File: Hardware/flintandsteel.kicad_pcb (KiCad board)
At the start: 4 copper layers, 44 x 58 mm, 117 parts, among them J1 RBUS, J2 USB_C_Receptacle_USB2.0, J3 Conn_01x02_Male, J4 Conn_01x02_Male, J5 Conn_01x02_Male, J6 Conn_01x02_Male, Q1 BUK9M11-40EX, Q2 BUK9M11-40EX, Q3 BUK9M11-40EX, Q4 BUK9M11-40EX, U1 ESP32-S3, U2 SN65HVD230, U3 LM66200DRLR, U4 MAX77827AEFD+T, U5 SC4215, U6 LTV-247, U7 INA219AxDCN, Y1 R940000171

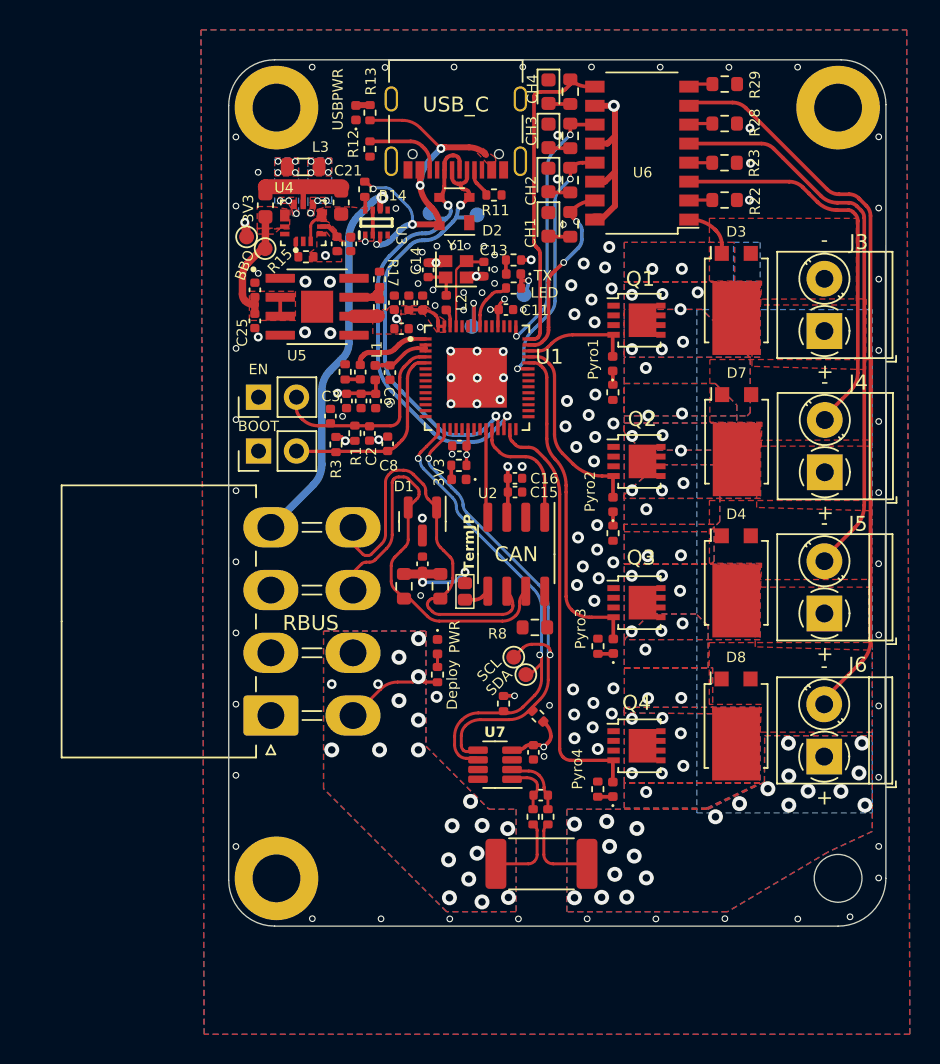
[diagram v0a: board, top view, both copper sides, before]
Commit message: added high side switch
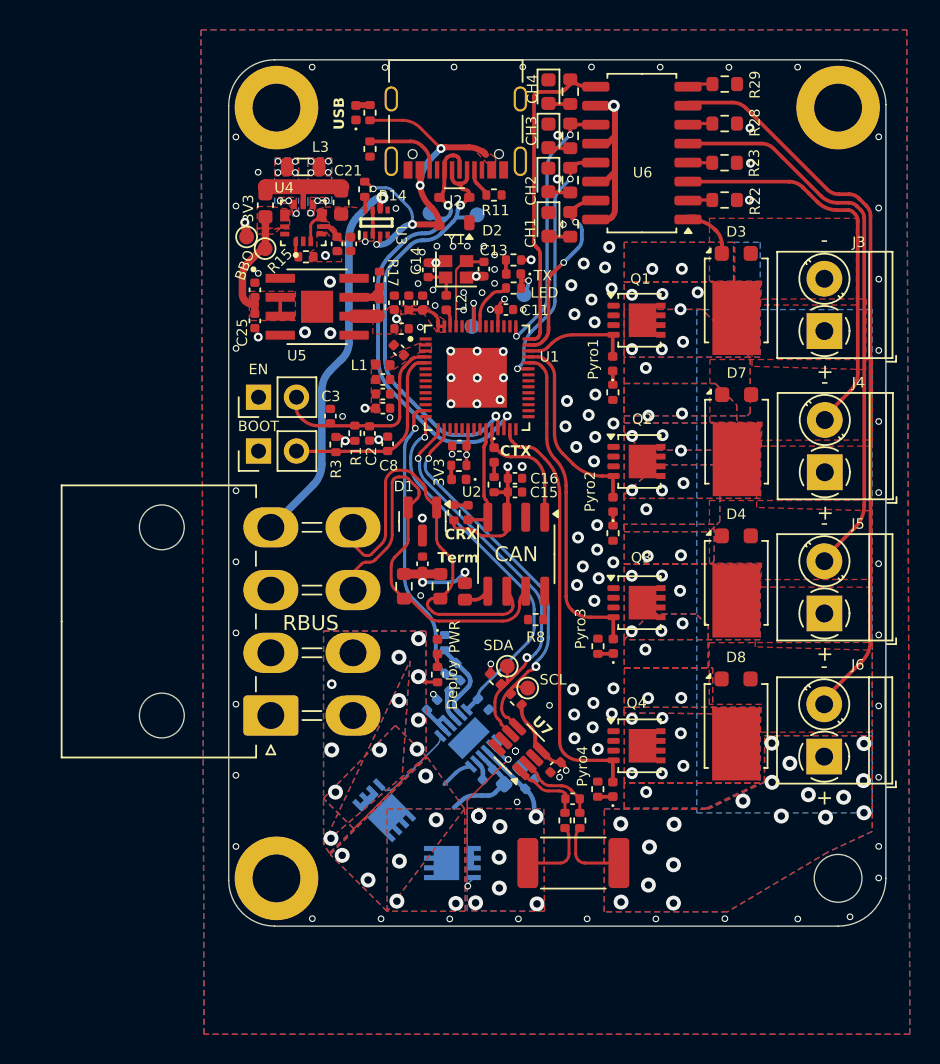
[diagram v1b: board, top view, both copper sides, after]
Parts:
- added C28: 0.1uF, Capacitor_SMD:C_0603_1608Metric, B.Cu at (125.0, 114.9)
- added C29: 0.1uF, Capacitor_SMD:C_0402_1005Metric, B.Cu at (119.6, 110.2)
- added C30: 0.1uF, Capacitor_SMD:C_0402_1005Metric, B.Cu at (126.2, 115.5)
- added CANRXLED1: ORANGE_LED, LED_SMD:LED_0402_1005Metric, F.Cu at (122.0, 97.3)
- added CANTXLED1: GREEN_LED, LED_SMD:LED_0402_1005Metric, F.Cu at (123.8, 93.5)
- added Q5: BSZ025N04LS, iclr:BSZ025N04LS, B.Cu at (116.4, 117.2)
- added Q6: BSZ025N04LS, iclr:BSZ025N04LS, B.Cu at (121.0, 120.8)
- added R30: 1k, Resistor_SMD:R_0402_1005Metric, F.Cu at (121.1, 97.3)
- added R37: R_Small, Resistor_SMD:R_0402_1005Metric, B.Cu at (121.1, 108.9)
- added R38: R_Small, Resistor_SMD:R_0402_1005Metric, B.Cu at (120.9, 107.7)
- added R39: R_Small, Resistor_SMD:R_0402_1005Metric, B.Cu at (120.5, 106.0)
- added R7: 1k, Resistor_SMD:R_0402_1005Metric, F.Cu at (123.8, 95.4)
- added U8: LM74810, iclr:SON50P300X300X80-13N-D, B.Cu at (122.1, 112.4)
- C12: value DNP -> 1uF; moved to B.Cu
- J2: footprint Connector_USB:USB_C_Receptacle_Palconn_UTC16-G -> iclr:USB_C_Receptacle_Palconn_UTC16-G
- R5: value DNP -> 10k; moved to B.Cu
- R8: footprint Resistor_SMD:R_0603_1608Metric -> Resistor_SMD:R_0402_1005Metric
- USBLED1: footprint Diode_SMD:D_0402_1005Metric -> LED_SMD:LED_0402_1005Metric
- Y1: footprint Crystal:Crystal_SMD_2016-4Pin_2.0x1.6mm -> iclr:Crystal_SMD_2016-4Pin_2.0x1.6mm
- moved C12 28.3 mm to (123.4, 114.9), turned to -135 degrees
- moved R5 24.1 mm to (123.0, 110.1), turned to -45 degrees
- moved C1 2.48 mm to (116.3, 90.3), turned to 0 degrees
- moved TP3 2.27 mm to (126.0, 109.1)
- moved C19 2.15 mm to (129.0, 116.5)
- moved R34 2.15 mm to (128.5, 117.9)
- moved R35 2.15 mm to (129.5, 117.9)
- moved R33 2.14 mm to (129.1, 120.8)
- moved U7 1.93 mm to (125.5, 113.1), turned to 135 degrees
- moved R32 1.83 mm to (125.2, 109.8)
- moved C18 1.79 mm to (127.9, 114.4), turned to -135 degrees
- moved R31 1.75 mm to (123.9, 108.4), turned to -45 degrees
- moved C6 1.61 mm to (117.4, 86.4), turned to 135 degrees
- moved C4 1.53 mm to (116.3, 89.4), turned to 0 degrees
- moved C5 1.52 mm to (116.3, 88.4), turned to 0 degrees
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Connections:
- net Net-(U7-IN+) renamed /SHNT_IN+
- net Net-(U7-IN-) renamed /SHNT_IN-
- C12 pad 1: Net-(C12-Pad1) -> /High side master switch/C
- C12 pad 2: Net-(U1-LNA_IN/RF) -> /High side master switch/CAP
- R33 pad 1: /DeployV -> /DeployV_Post_Diode
- R34 pad 1: /DeployV -> /DeployV_Post_Diode
- R5 pad 1: GND -> /HSIDE_EN
- R5 pad 2: Net-(C12-Pad1) -> GND
- U1 pad 1: Net-(U1-LNA_IN/RF) -> unconnected-(U1-LNA_IN/RF-Pad1)
- U1 pad 13: unconnected-(U1-GPIO8/ADC1_CH7-Pad13) -> /BUS_VMON
- U1 pad 14: unconnected-(U1-GPIO9/ADC1_CH8-Pad14) -> /HSIDE_EN
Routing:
- net /HSIDE_EN: track 0.00 -> 25.1 mm, vias 0 -> 1
- net /BUS_VMON: track 0.00 -> 20.4 mm, vias 0 -> 1
- net /High side master switch/HGate: track 0.00 -> 11.8 mm, vias 0 -> 2
- net /DeployV_Post_Diode: track 0.00 -> 11.0 mm, vias 0 -> 8
- net /High side master switch/C: track 0.00 -> 9.11 mm, vias 0 -> 7
- net /SCL: track 34.2 -> 26.4 mm
- net /DeployV: track 12.0 -> 5.45 mm, vias 20 -> 11
- net /High side master switch/DGate: track 0.00 -> 5.91 mm
- net Net-(U8-OV): track 0.00 -> 5.45 mm
- net +3V3: track 37.9 -> 43.1 mm
- net Net-(U1-LNA_IN/RF): track 5.21 -> 0.00 mm
- net /SDA: track 32.5 -> 27.5 mm
- net Net-(C6-Pad1): track 4.66 -> 0.00 mm
- net Net-(U8-SW): track 0.00 -> 2.22 mm
- net /CAN_RX: track 5.77 -> 7.39 mm
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- added copper zone on B.Cu, net /DeployV_Post_Diode
- added copper zone on F.Cu, net /DeployV_Post_Diode
- added copper zone on B.Cu, net /High side master switch/C
- added copper zone on F.Cu, net /High side master switch/C
- added copper zone on F.Cu, net Net-(C6-Pad1)
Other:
- board text added: "CRX"
- board text added: "CTX"
- board text added: "Designed By Andrei Paduraru Electronics 2024"
- board text added: "FLINT & STEEL v3.0"
- board text added: "USB"
- board text removed: "Designed By Andrei Paduraru Electronics and Payload 2023"
- board text removed: "locked"

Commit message: v3 hardware I guess
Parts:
- added 16VLED2: ORANGE_LED, LED_SMD:LED_0402_1005Metric, F.Cu at (143.0, 123.5)
- added D11: S-102T, iclr:SODFL3516X70N, F.Cu at (140.1, 68.8)
- added D12: S-102T, iclr:SODFL3516X70N, F.Cu at (140.1, 73.8)
- added D13: S-102T, iclr:SODFL3516X70N, F.Cu at (140.1, 76.5)
- added D14: S-102T, iclr:SODFL3516X70N, F.Cu at (140.1, 71.3)
- added D15: V8PAM10S-M3/I, iclr:V8PAM10SM3I, B.Cu at (143.0, 93.3)
- added D16: V8PAM10S-M3/I, iclr:V8PAM10SM3I, B.Cu at (143.0, 83.7)
- added D17: V8PAM10S-M3/I, iclr:V8PAM10SM3I, B.Cu at (142.9, 102.6)
- added D18: V8PAM10S-M3/I, iclr:V8PAM10SM3I, B.Cu at (142.9, 112.2)
- added G***: LOGO, iclr:rae_logo_4mm, F.Cu at (109.2, 116.3)
- added G***: LOGO, iclr:rae_logo_8mm, B.Cu at (135.9, 110.3)
- added R40: 3k, Resistor_SMD:R_0402_1005Metric, F.Cu at (141.0, 123.1)
- Q1, Q2, Q3, Q4: value BUK9M11-40EX -> BSZ025N04LS; footprint Package_TO_SOT_SMD:LFPAK33 -> iclr:BSZ025N04LS
- R22, R23, R28, R29: value 10k -> 10K; footprint Resistor_SMD:R_0603_1608Metric -> Resistor_SMD:R_0402_1005Metric
- moved R28 44.1 mm to (129.8, 114.4), turned to -90 degrees
- moved R29 37.4 mm to (129.9, 104.8), turned to -90 degrees
- moved G*** 34.3 mm to (112.6, 83.1)
- moved R23 24.4 mm to (130.7, 96.8), turned to -90 degrees
- moved R22 12.9 mm to (130.5, 85.9), turned to -90 degrees
- moved G*** 0.30 mm to (130.5, 90.7)
- turned Q1 to -90 degrees
- turned Q2 to -90 degrees
- turned Q3 to -90 degrees
- turned Q4 to -90 degrees
- renumbered D5 to D10, D10 to D5, D9 to D6, D6 to D9, R27 to R20, R26 to R21, R21 to R26, R20 to R27
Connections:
- net /Cont 4 renamed /Cont 0
- D3 pad 1: Net-(J3-Pin_2) -> Net-(D16-A)
- D3 pad 2: Net-(J3-Pin_2) -> Net-(D16-A)
- D4 pad 1: Net-(J5-Pin_2) -> Net-(D17-A)
- D4 pad 2: Net-(J5-Pin_2) -> Net-(D17-A)
- D7 pad 1: Net-(J4-Pin_2) -> Net-(D15-A)
- D7 pad 2: Net-(J4-Pin_2) -> Net-(D15-A)
- D8 pad 1: Net-(J6-Pin_2) -> Net-(D18-A)
- D8 pad 2: Net-(J6-Pin_2) -> Net-(D18-A)
- Firing1 pad 2: /Nuke 1 -> /Nuke 0
- Firing2 pad 2: /Nuke 2 -> /Nuke 1
- Firing3 pad 2: /Nuke 3 -> /Nuke 2
- Firing4 pad 2: /Nuke 4 -> /Nuke 3
- J3 pad 2: Net-(J3-Pin_2) -> Net-(D16-A)
- J4 pad 2: Net-(J4-Pin_2) -> Net-(D15-A)
- J5 pad 2: Net-(J5-Pin_2) -> Net-(D17-A)
- J6 pad 2: Net-(J6-Pin_2) -> Net-(D18-A)
- Q1 pad 4: /Nuke 1 -> /Nuke 0
- Q2 pad 4: /Nuke 2 -> /Nuke 1
- Q3 pad 4: /Nuke 3 -> /Nuke 2
- Q4 pad 4: /Nuke 4 -> /Nuke 3
- R21 pad 1: /Cont 3 -> /Cont 1
- R22 pad 1: Net-(R22-Pad1) -> /Nuke 0
- R23 pad 1: Net-(R23-Pad1) -> /Nuke 1
- R27 pad 1: /Cont 1 -> /Cont 3
- R28 pad 1: Net-(R28-Pad1) -> /Nuke 3
- R29 pad 1: Net-(R29-Pad1) -> /Nuke 2
- U1 pad 27: /Nuke 4 -> /Nuke 3
- U1 pad 38: /Nuke 3 -> /Nuke 2
- U1 pad 39: /Nuke 2 -> /Nuke 1
- U1 pad 40: /Nuke 1 -> /Nuke 0
- U1 pad 41: /Cont 1 -> /Cont 3
- U1 pad 43: /Cont 3 -> /Cont 1
- U6 pad 1: Net-(J3-Pin_2) -> Net-(D18-A)
- U6 pad 11: /Cont 3 -> /Cont 1
- U6 pad 15: /Cont 1 -> /Cont 3
- U6 pad 2: Net-(R22-Pad1) -> Net-(D13-A)
- U6 pad 3: Net-(J4-Pin_2) -> Net-(D17-A)
- U6 pad 4: Net-(R23-Pad1) -> Net-(D12-A)
- U6 pad 5: Net-(J5-Pin_2) -> Net-(D15-A)
- U6 pad 6: Net-(R28-Pad1) -> Net-(D14-A)
- U6 pad 7: Net-(J6-Pin_2) -> Net-(D16-A)
- U6 pad 8: Net-(R29-Pad1) -> Net-(D11-A)
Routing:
- net Net-(J6-Pin_2): track 49.2 -> 0.00 mm
- net Net-(D18-A): track 0.00 -> 48.5 mm, vias 0 -> 2
- net Net-(J5-Pin_2): track 37.5 -> 0.00 mm
- net Net-(D17-A): track 0.00 -> 37.1 mm, vias 0 -> 2
- net /Nuke 4: track 28.4 -> 0.00 mm
- net Net-(D15-A): track 0.00 -> 27.7 mm
- net Net-(J4-Pin_2): track 26.3 -> 0.00 mm
- net Net-(D16-A): track 0.00 -> 14.8 mm
- net /Nuke 2: track 13.1 -> 22.2 mm
- net /Nuke 0: track 0.00 -> 7.48 mm
- net /Nuke 1: track 7.48 -> 14.1 mm
- net /Nuke 3: track 22.2 -> 28.4 mm
- net /Cont 3: track 18.0 -> 12.8 mm
- net /Cont 1: track 12.8 -> 18.0 mm
- net Net-(J3-Pin_2): track 4.35 -> 0.00 mm
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- added copper zone on B.Cu, net Net-(D15-A)
- added copper zone on F.Cu, net Net-(D15-A)
- added copper zone on B.Cu, net Net-(D16-A)
- added copper zone on F.Cu, net Net-(D16-A)
- added copper zone on B.Cu, net Net-(D17-A)
- added copper zone on F.Cu, net Net-(D17-A)
- added copper zone on B.Cu, net Net-(D18-A)
- added copper zone on F.Cu, net Net-(D18-A)
- removed copper zone on F.Cu, net Net-(J3-Pin_2)
- removed copper zone on F.Cu, net Net-(J4-Pin_2)
- removed copper zone on F.Cu, net Net-(J5-Pin_2)
- removed copper zone on F.Cu, net Net-(J6-Pin_2)
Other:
- board text removed: "Batch Number - JLCJLCJLCJLC"

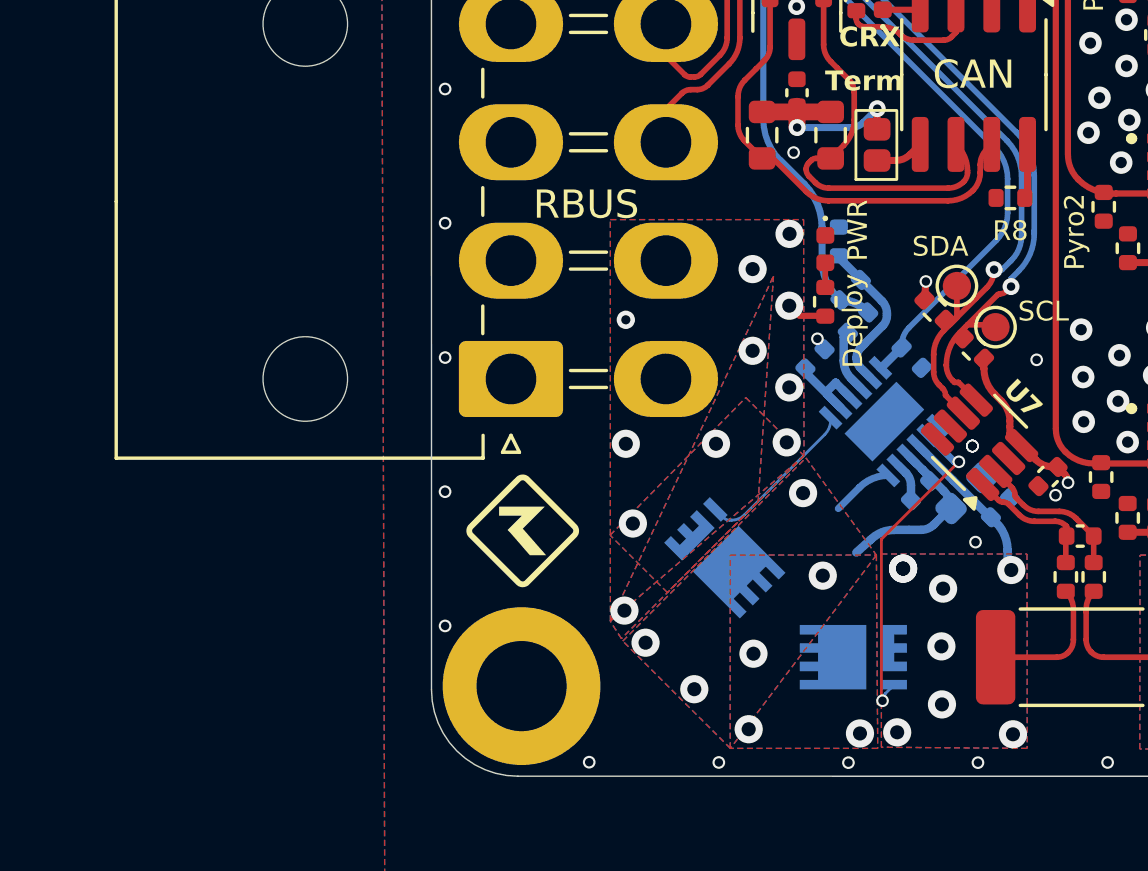
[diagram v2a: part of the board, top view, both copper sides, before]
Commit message: forgot teardrops
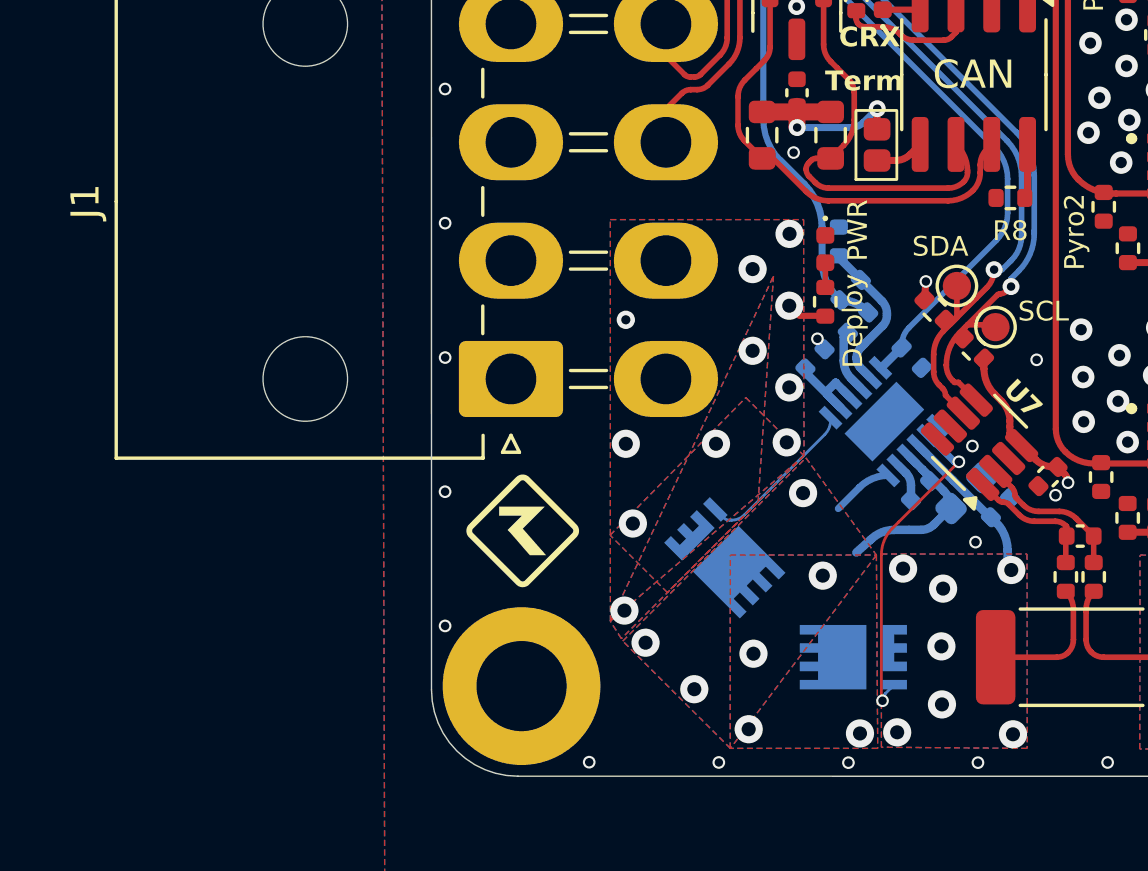
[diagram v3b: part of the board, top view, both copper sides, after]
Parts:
- J1: footprint Connector_Molex:Molex_Mini-Fit_Jr_5569-08A2_2x04_P4.20mm_Horizontal -> iclr:Molex_Mini-Fit_Jr_5569-08A2_2x04_P4.20mm_Horizontal
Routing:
- net GND: vias 126 -> 123
- net /DeployV_Post_Diode: vias 8 -> 7

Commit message: TVS diode and sized resistor ladder
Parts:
- added D19: P6SMBJ28CA, Diode_SMD:D_SMA, B.Cu at (119.3, 105.9)
- R37: value R_Small -> 100k
- R38: value R_Small -> 5.1k
- R39: value R_Small -> 4.22k
- moved G*** 4.40 mm to (139.1, 107.3)
- moved R39 2.54 mm to (122.5, 107.5), turned to -135 degrees
- moved G*** 0.33 mm to (112.8, 83.3)
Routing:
- net /BUS_VMON: track 20.4 -> 22.9 mm
- net Net-(U8-OV): track 5.45 -> 4.42 mm
- net GND: vias 123 -> 124
